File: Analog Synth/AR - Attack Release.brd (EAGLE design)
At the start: 160 x 100 mm, 44 parts, among them IC1 78L05Z, IC2 TL084P, T1 2N3904, T2 2N3904, T3 2N3904, T4 2N3904, T5 2N3904

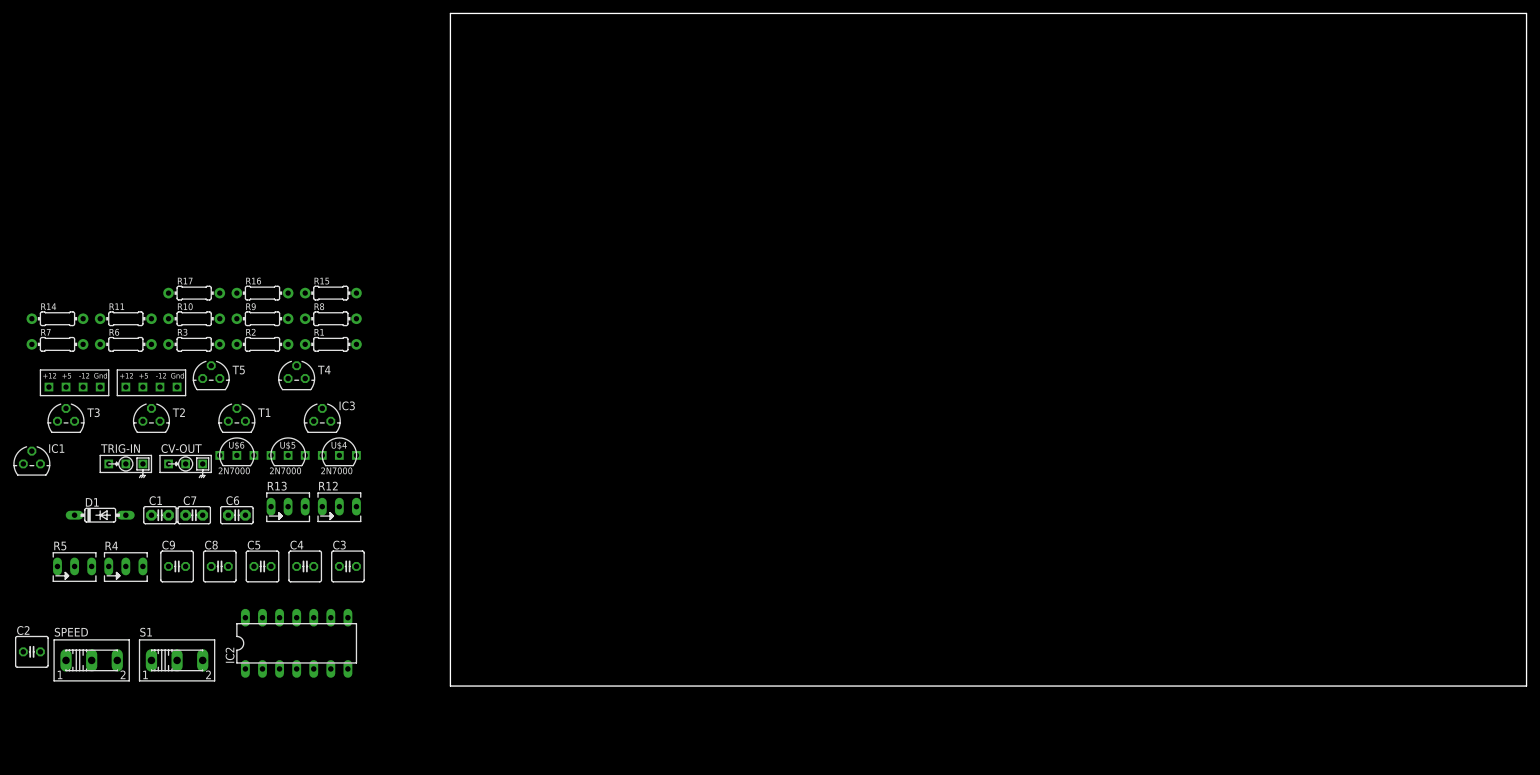
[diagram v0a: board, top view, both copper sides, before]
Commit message: added Attack-Release schematic with a JFET-based VCA that won't work. I will need to modify the schematic for a bual board.
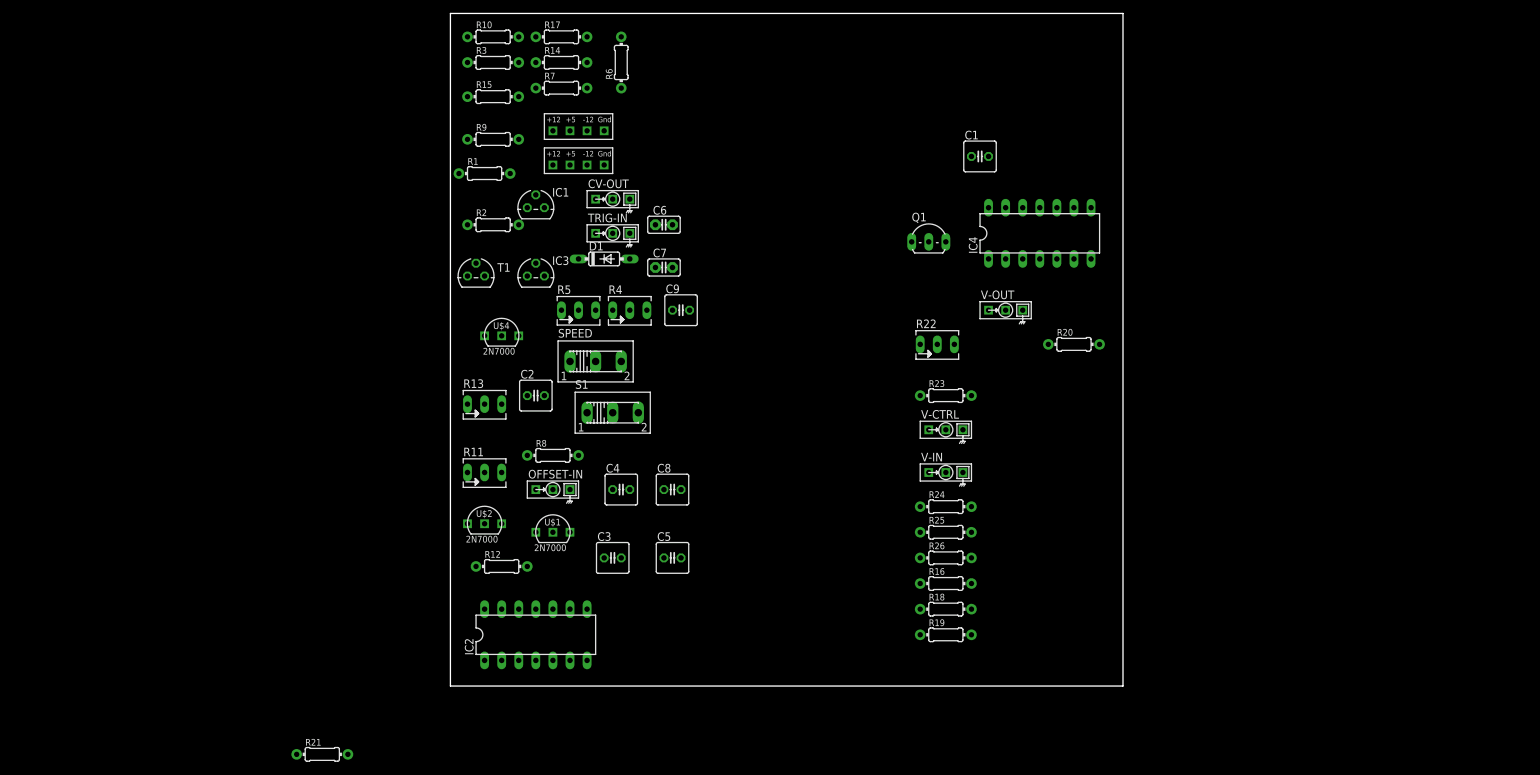
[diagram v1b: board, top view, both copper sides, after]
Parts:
- removed T2, T3, T4, T5: 2N3904, transistor:TO92
- removed U$5, U$6: 2N7000, !synth_sch:2N7000
- added IC4: TL084P, linear:DIL14
- added OFFSET-IN, V-CTRL, V-IN, V-OUT: I/O, !synth_sch:MONO_JACK
- added Q1: 2N5485, transistor-fet:TO92-
- added R18, R19, R25: 100k, resistor:0204/7
- added R20, R23: 1k, resistor:0204/7
- added R21: 220k, resistor:0204/7
- added R22: 100k, pot:B64Y
- added R24: 10k, resistor:0204/7
- added R26: 68.8k, resistor:0204/7
- added U$1, U$2: 2N7000, !synth_sch:2N7000
- C1: value 0.1µ -> 1µ; device capacitor-wima:C2.5-2 -> rcl:C025-050X050
- C8: value 10µ -> 33µ
- C9: value 1m -> 1000u
- R11: value 47k -> 10k; device resistor:0204/7 -> pot:B64Y
- R12: device pot:B64Y -> resistor:0204/7
- moved C1 133.1 mm to (78.7, 78.7)
- moved R16 110.4 mm to (73.7, 15.2)
- moved SPEED 87.1 mm to (21.6, 48.3)
- moved R6 84.7 mm to (25.4, 92.7), turned to 90 degrees
- moved C9 84.1 mm to (34.3, 55.9)
- moved D1 84.1 mm to (22.9, 63.5)
- moved R14 84.1 mm to (16.5, 92.7)
- moved R4 84.1 mm to (26.7, 55.9)
- moved R5 84.1 mm to (19.1, 55.9)
- moved R7 84.1 mm to (16.5, 88.9)
- moved U$7 84.1 mm to (19.1, 82.5)
- moved C2 84.1 mm to (12.7, 43.2)
- moved IC1 84.1 mm to (12.7, 71.1)
- moved TRIG-IN 80.1 mm to (24.1, 67.3)
- moved C7 79.0 mm to (31.8, 62.2)
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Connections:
- removed net N$22: IC2.14, R16.2, R17.1
- new net N$24: IC4.8, R16.1, R19.2
- new net N$27: Q1.1, R19.1
- new net N$28: IC2.12, OFFSET-IN.P$2
- new net N$29: R20.2, V-OUT.P$2
- new net N$30: R22.A, R23.2
- new net N$31: IC4.5, V-IN.P$2
- new net N$32: IC4.6, IC4.7, Q1.3, R26.2
- new net N$33: IC4.3, V-CTRL.P$2
- new net N$34: IC4.12, Q1.2, R24.2
- new net N$35: IC4.10, R21.2, R25.2, R26.1
- new net N$36: IC4.13, IC4.14, R20.1
- net +12V: no longer T2.1, T3.1, T4.1, T5.1
- net -12V: now also R21.1
- net GND: now also OFFSET-IN.P$1, OFFSET-IN.P$3, R11.E, R18.1, R23.1, R24.1, U$1.S, U$2.S, V-CTRL.P$1, V-CTRL.P$3, V-IN.P$1, V-IN.P$3, V-OUT.P$1; no longer IC2.12, R8.1, U$5.S, U$6.S
- net N$13: now also IC2.13, IC2.14, R12.1; no longer T2.3, T3.2
- net N$14: now also IC4.1, R22.S, R25.1; no longer T4.3, T5.2
- net N$16: now also IC4.9, R16.2, R18.2; no longer IC2.5, R8.2, T5.3
- net N$17: now also R11.S; no longer IC2.6, IC2.7
- net N$19: now also R8.1; no longer R11.1
- net N$20: now also R12.2, R14.2, R15.1, R8.2; no longer R11.2, R12.A
- net N$23: now also R17.1; no longer R12.E, R12.S
- net N$3: now also U$1.G, U$2.G; no longer U$5.G, U$6.G
- net N$4: now also U$1.D; no longer U$5.D
- net N$5: now also IC4.2, R22.E; no longer IC2.13, R14.2, R15.1, R16.1
- net N$6: now also IC2.6, IC2.7, R11.A; no longer T3.3, T4.2
- net N$7: now also U$2.D; no longer U$6.D
- net N$8: now also IC2.5; no longer T2.2
- net V+: now also IC4.4
- net V-: now also IC4.11
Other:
- board size 160 x 100 mm -> 100 x 100 mm
